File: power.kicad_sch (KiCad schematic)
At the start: 4 parts, among them J3 Power Input

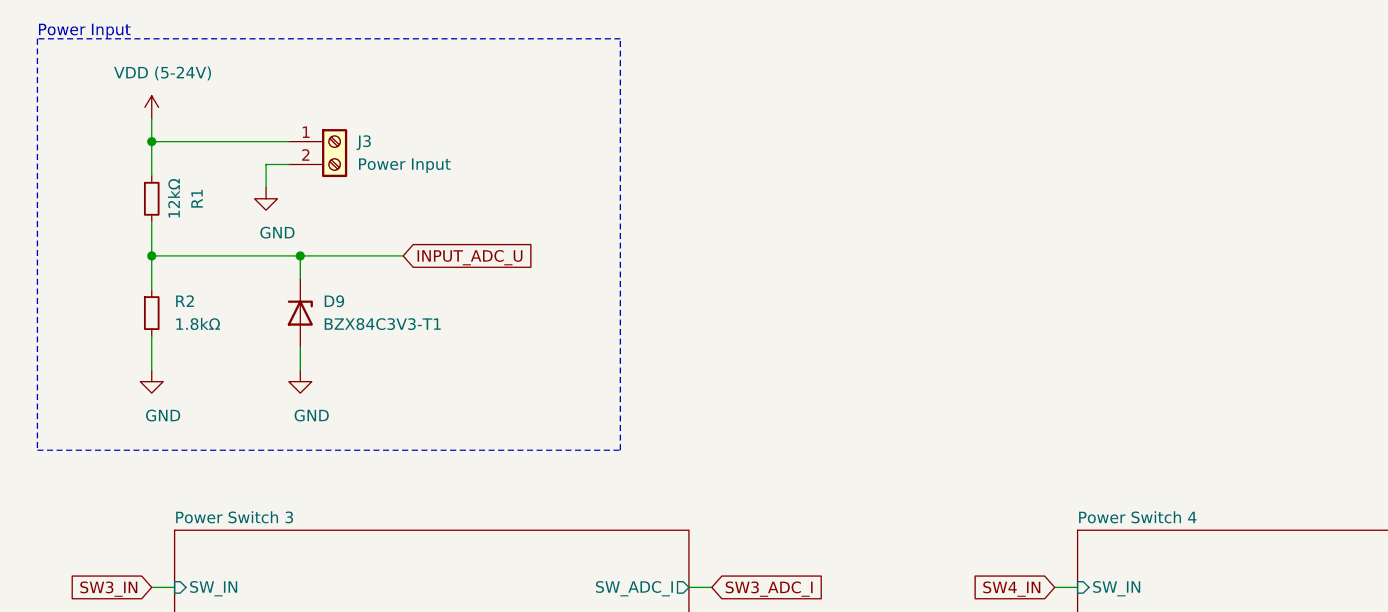
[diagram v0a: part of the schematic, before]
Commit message: initial component placement
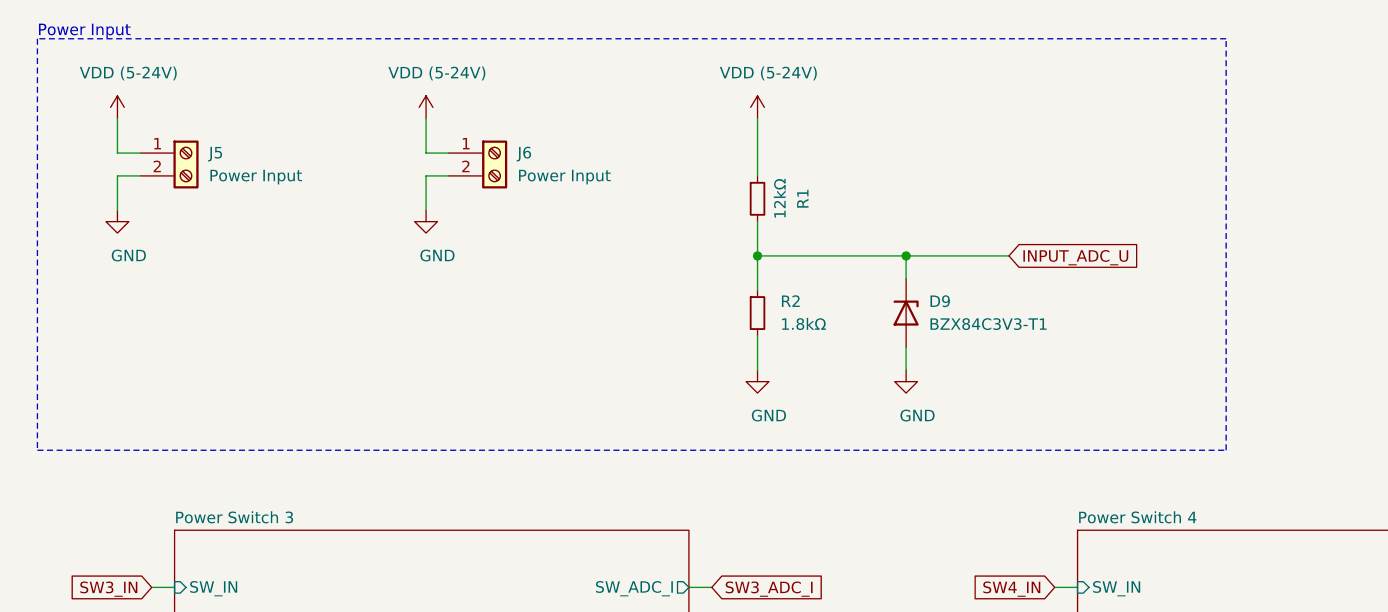
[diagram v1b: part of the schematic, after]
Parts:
- removed J3: Power Input, TerminalBlock_RND:TerminalBlock_RND_205-00287_1x02_P5.08mm_Horizontal, symbol Connector:Screw_Terminal_01x02
- added J5, J6: Power Input, TerminalBlock_RND:TerminalBlock_RND_205-00287_1x02_P5.08mm_Horizontal, symbol Connector:Screw_Terminal_01x02
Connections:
- net GND: now also J5.2 (Pin_2), J6.2 (Pin_2)
- net VDD: now also J5.1 (Pin_1), J6.1 (Pin_1)
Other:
- moved on the sheet: D9, R1, R2

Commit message: updated footprints, adjustments in placement
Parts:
- J5, J6: footprint TerminalBlock_RND:TerminalBlock_RND_205-00287_1x02_P5.08mm_Horizontal -> TerminalBlock_RND:TerminalBlock_RND_205-00045_1x02_P5.00mm_Horizontal
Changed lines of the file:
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@@
       (effects (font (size 1.27 1.27)) (justify left))
     )
-    (property "Footprint" "TerminalBlock_RND:TerminalBlock_RND_205-00287_1x02_P5.08mm_Horizontal" (id 2) (at 35.56 31.75 0)
+    (property "Footprint" "TerminalBlock_RND:TerminalBlock_RND_205-00045_1x02_P5.00mm_Horizontal" (id 2) (at 35.56 31.75 0)
       (effects (font (size 1.27 1.27)) hide)
     )
@@
       (effects (font (size 1.27 1.27)) (justify left))
     )
-    (property "Footprint" "TerminalBlock_RND:TerminalBlock_RND_205-00287_1x02_P5.08mm_Horizontal" (id 2) (at 69.85 31.75 0)
+    (property "Footprint" "TerminalBlock_RND:TerminalBlock_RND_205-00045_1x02_P5.00mm_Horizontal" (id 2) (at 69.85 31.75 0)
       (effects (font (size 1.27 1.27)) hide)
     )

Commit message: use 1% resistor for voltage divider, add one more fiducial
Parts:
- R1: value 12kΩ -> 12kΩ 1%
- R2: value 1.8kΩ -> 1.8kΩ 1%
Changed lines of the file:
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@@
     (in_bom yes) (on_board yes)
     (property "Reference" "R1" (id 0) (at 104.14 36.83 90))
-    (property "Value" "12kΩ" (id 1) (at 101.6 36.83 90))
+    (property "Value" "12kΩ 1%" (id 1) (at 101.6 36.83 90))
     (property "Footprint" "Resistor_SMD:R_0603_1608Metric" (id 2) (at 99.06 36.83 0)
       (effects (font (size 1.27 1.27)) hide)
@@
       (effects (font (size 1.27 1.27)) (justify left))
     )
-    (property "Value" "1.8kΩ" (id 1) (at 101.6 50.8 0)
+    (property "Value" "1.8kΩ 1%" (id 1) (at 101.6 50.8 0)
       (effects (font (size 1.27 1.27)) (justify left))
     )
